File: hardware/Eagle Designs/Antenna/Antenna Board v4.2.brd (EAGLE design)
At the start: 100 x 100 mm, 18 parts, among them J1 5037630291, J10 MCX-J-P-X-ST-TH1, J11 U.FL-R-SMT-1(01), J12 MCX-J-P-X-ST-TH1, J13 MCX-J-P-X-ST-TH1, J14 MOLEX_503763-0491MOLEX_503763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, J15 MOLEX_503763-0491MOLEX_503763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, J2 503763-0591, J3 MOLEX_503763-0491MOLEX_503763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, J4 MOLEX_503763-0291MOLEX_503763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

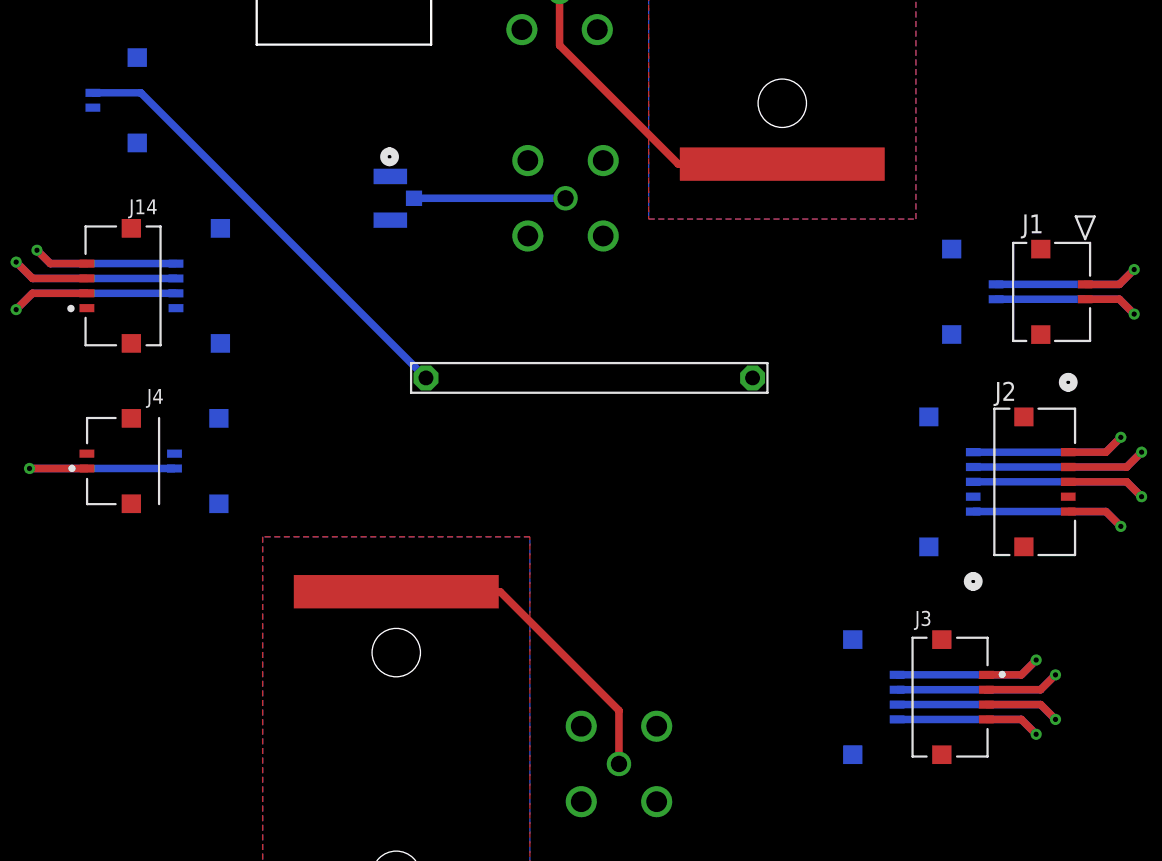
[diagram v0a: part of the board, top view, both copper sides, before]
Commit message: Made edits to solar panel, antenna, battery boards
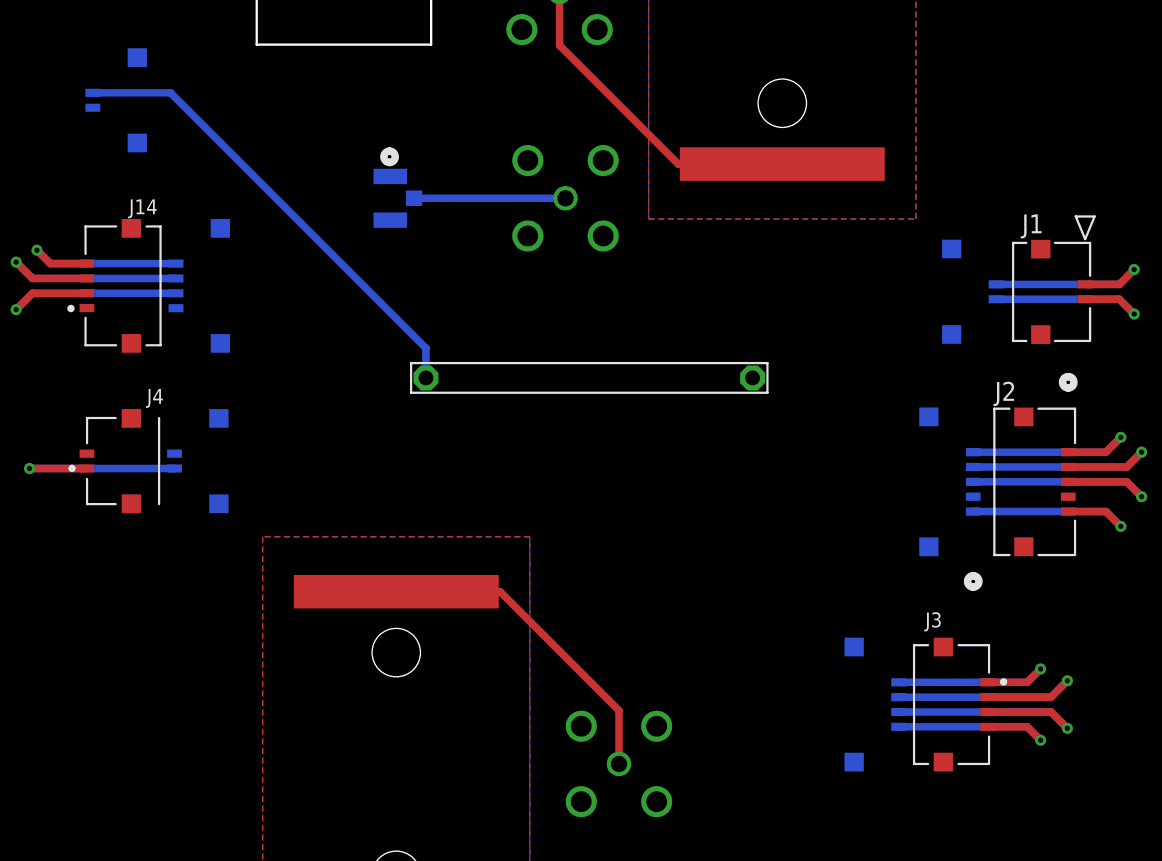
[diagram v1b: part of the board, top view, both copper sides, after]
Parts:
- moved J3 0.51 mm to (74.4, 28.0)
- moved J7 0.51 mm to (68.4, 28.0)
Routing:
- net TX+: track 16.2 -> 17.6 mm
- net RX-: track 16.2 -> 17.6 mm
- net VCC_BURN: track 30.4 -> 31.6 mm
